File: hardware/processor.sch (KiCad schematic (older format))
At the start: 17 parts, among them J1 USB_2, U1 ATMEGA32U4, X1 16 MHz

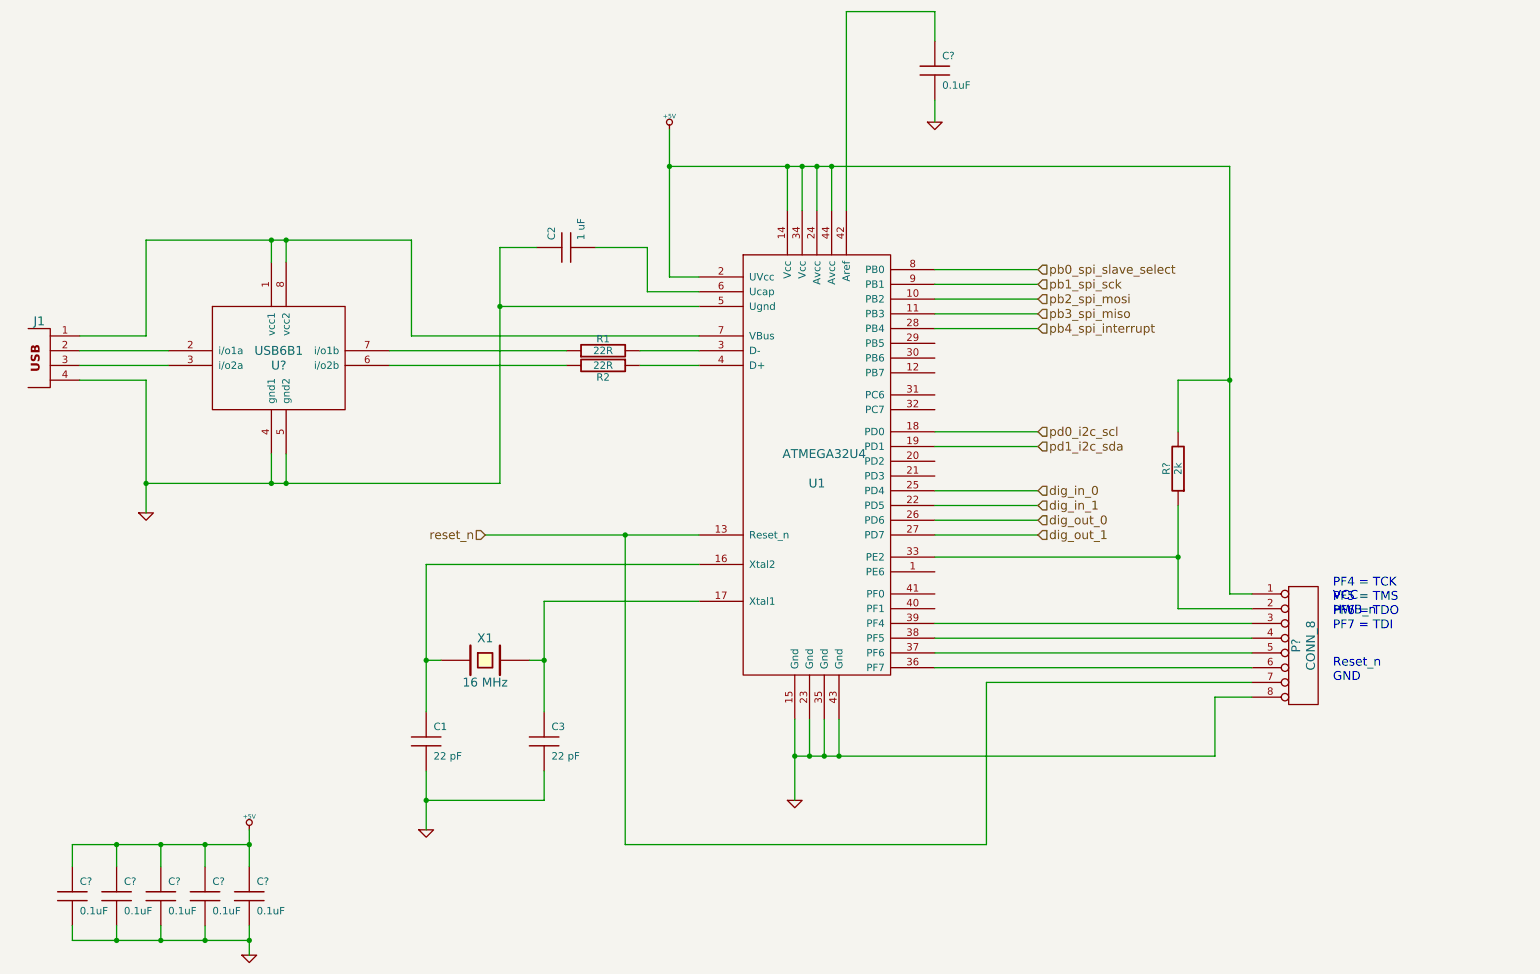
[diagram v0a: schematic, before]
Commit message: rearranged some processor I/O pins and added LEDs
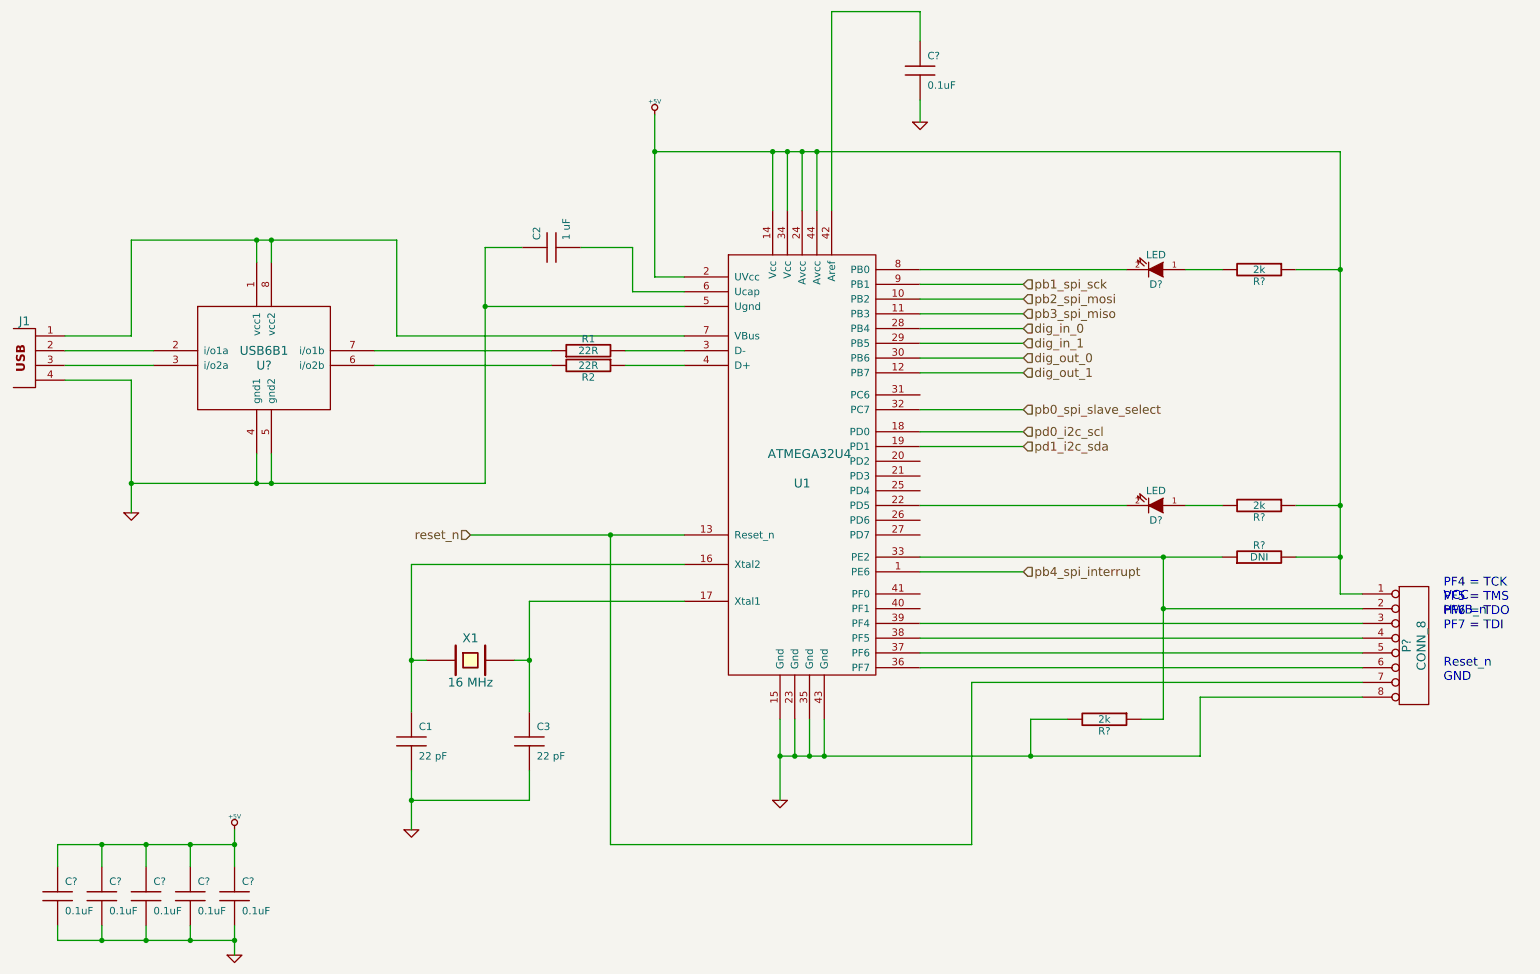
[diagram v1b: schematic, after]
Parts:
- added D? (x2): LED, symbol LED
- added R? (x3): 2k, symbol R
- R?: value 2k -> DNI
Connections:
- net +5V: now also R?.1, R?.1
- net GND: now also R?.2
- net dig_in_0: now also U1.28 (PB4); no longer U1.25 (PD4)
- net dig_in_1: now also U1.29 (PB5); no longer U1.22 (PD5)
- net dig_out_0: now also U1.30 (PB6); no longer U1.26 (PD6)
- net dig_out_1: now also U1.12 (PB7); no longer U1.27 (PD7)
- net pb0_spi_slave_select: now also U1.32 (PC7); no longer U1.8 (PB0)
- net pb4_spi_interrupt: now also U1.1 (PE6); no longer U1.28 (PB4)
- net at P?.2 (P2), R?.1, U1.33 (PE2): now also R?.1
- new net: D?.2 (K), U1.22 (PD5)
- new net: D?.2 (K), U1.8 (PB0)
- new net: D?.1 (A), R?.2 (x2)
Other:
- moved on the sheet: C1, C2, C3, C?, J1, P?, R1, R2, R?, U1, U?, X1

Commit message: changed heirarchy labels, changed diode and inductor to standard library symbols
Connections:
- net pb0_spi_slave_select renamed spi_slave_select
- net pb1_spi_sck renamed spi_sck
- net pb2_spi_mosi renamed spi_mosi
- net pb3_spi_miso renamed spi_miso
- net pb4_spi_interrupt renamed spi_interrupt
- net pd0_i2c_scl renamed i2c_scl
- net pd1_i2c_sda renamed i2c_sda
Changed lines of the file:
@@
-EESchema Schematic File Version 2  date Thu 31 Oct 2013 01:30:23 PM EDT
+EESchema Schematic File Version 2  date Mon 04 Nov 2013 07:38:03 AM EST
 LIBS:power
 LIBS:device
@@
 Sheet 5 5
 Title ""
-Date "31 oct 2013"
+Date "4 nov 2013"
 Rev ""
 Comp ""
@@
 $EndComp
 Text HLabel 7650 3700 2    60   Input ~ 0
-pd1_i2c_sda
+i2c_sda
 Text HLabel 7650 3600 2    60   Input ~ 0
-pd0_i2c_scl
+i2c_scl
 Text HLabel 7650 4550 2    60   Input ~ 0
-pb4_spi_interrupt
+spi_interrupt
 Text HLabel 7650 2800 2    60   Input ~ 0
-pb3_spi_miso
+spi_miso
 Text HLabel 7650 2700 2    60   Input ~ 0
-pb2_spi_mosi
+spi_mosi
 Text HLabel 7650 2600 2    60   Input ~ 0
-pb1_spi_sck
+spi_sck
 Text HLabel 7650 3450 2    60   Input ~ 0
-pb0_spi_slave_select
+spi_slave_select
 Text HLabel 3900 4300 0    60   Input ~ 0
 reset_n

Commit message: cleaned up most of the error check problems
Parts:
- gave numbers to parts that had none: 14
- renumbered C1 to C22, C3 to C23, C2 to C24, R1 to R40, R2 to R41, U1 to U10, X1 to X2
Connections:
- no-connect marks 0 -> 8

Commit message: Added ISP Programming header for microcontroller
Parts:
- added P4: CONN_3X2, symbol CONN_3X2
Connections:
- wire segments 98 -> 104
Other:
- note added: "ISP Programming\n"
